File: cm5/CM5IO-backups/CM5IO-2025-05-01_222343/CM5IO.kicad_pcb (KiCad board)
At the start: 4 copper layers, 101.9 x 90.8 mm, 67 parts, among them J1 67910-5700, J14 JST_SHBM04B-SRSS-TB, J2 B2B-XH-A_LF__SN_, J4 0786463001, J5 USB3_A, J6 Conn_02x03_Counter_Clockwise, J7 Conn_01x04, U2 TLV320ADC6120IRTER, U5 74LVC1G07SE-7, U6 AP22653W6, U8 AP3441SHE-7B

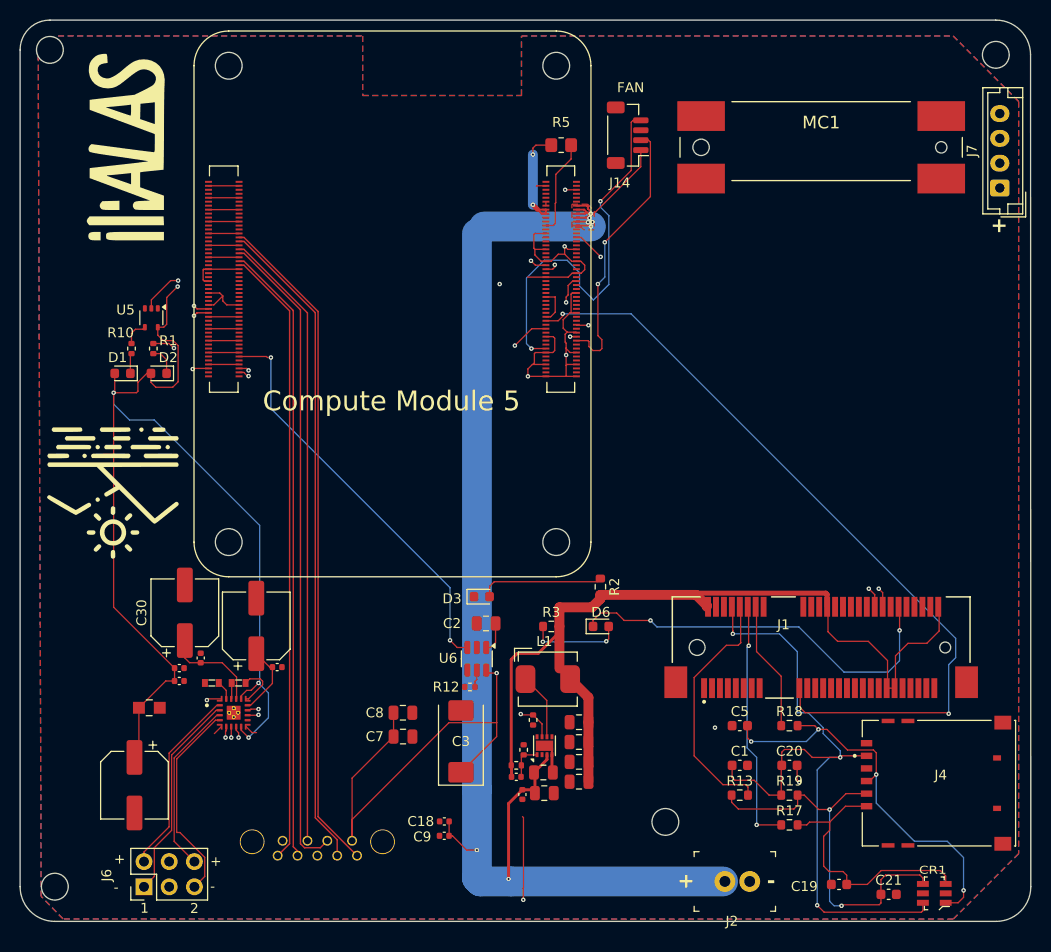
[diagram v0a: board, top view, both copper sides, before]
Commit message: Delete some unnecessary components and fix up some of the trace thicknesses
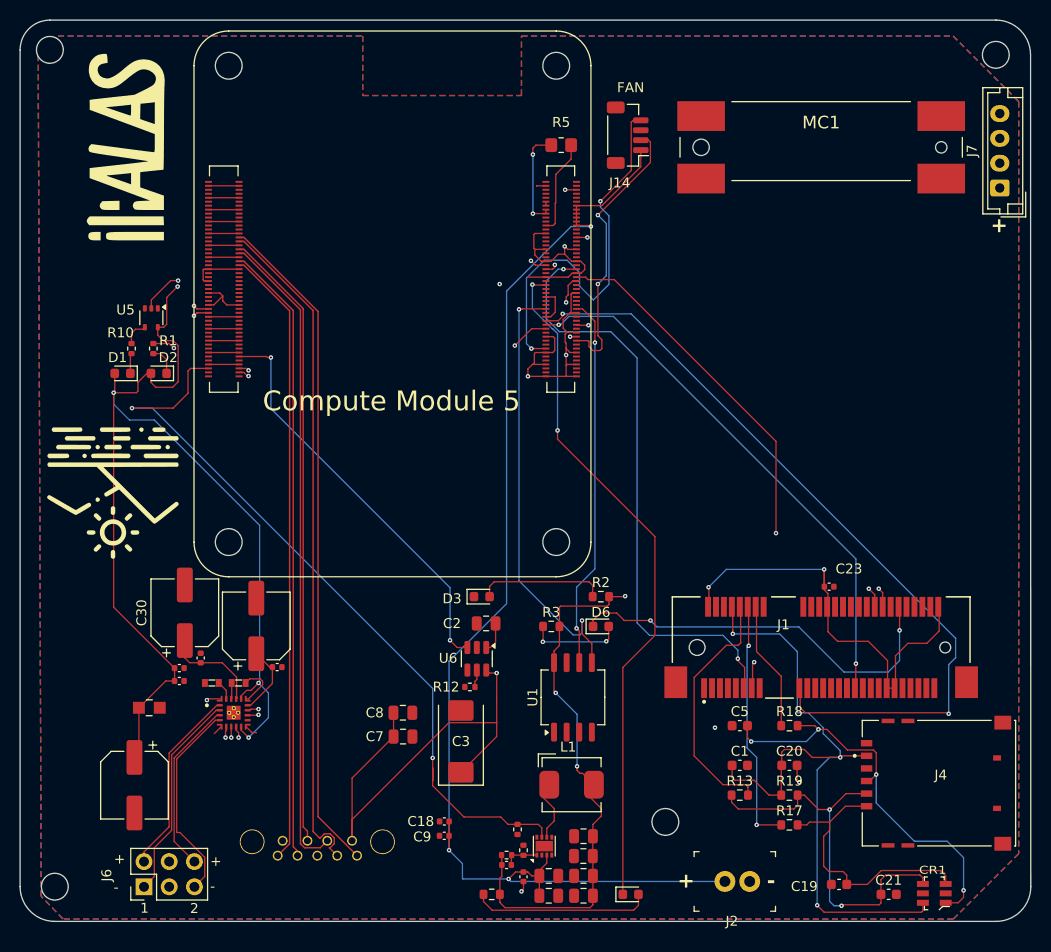
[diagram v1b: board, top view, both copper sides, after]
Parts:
- added C23: 100n, Capacitor_SMD:C_0402_1005Metric, F.Cu at (223.0, 126.0)
- added D4: LED Red, LED_SMD:LED_0603_1608Metric, F.Cu at (203.0, 157.0)
- added R11: 330, Resistor_SMD:R_0603_1608Metric, F.Cu at (189.0, 157.0)
- added U1: CAT24C128, Package_SO:SOIC-8_5.3x6.2mm_P1.27mm, F.Cu at (197.2, 137.2)
- moved C14 11.5 mm to (198.2, 151.1)
- moved C15 11.5 mm to (198.2, 157.1)
- moved C16 11.5 mm to (198.2, 155.1)
- moved C17 11.5 mm to (198.2, 153.1)
- moved R14 11.1 mm to (191.6, 150.5)
- moved L1 10.9 mm to (197.1, 145.9)
- moved C4 10.4 mm to (194.8, 155.1)
- moved C6 10.4 mm to (194.8, 157.1)
- moved R16 10.1 mm to (192.2, 152.6)
- moved U8 10.1 mm to (194.3, 152.1)
- moved R15 9.10 mm to (190.5, 153.0)
- moved C11 8.94 mm to (190.5, 154.0)
- moved C10 8.29 mm to (192.2, 155.2)
- moved R2 1.00 mm to (200.0, 127.0), turned to 0 degrees
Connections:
- J1 pad 11: unconnected-(J1-Pad11) -> /CM5_GPIO ( Ethernet, GPIO, SDCARD)/GPIO14
- J1 pad 13: unconnected-(J1-Pad13) -> /CM5_GPIO ( Ethernet, GPIO, SDCARD)/GPIO15
- J1 pad 31: /PCIe-M2/DTR -> /CM5_GPIO ( Ethernet, GPIO, SDCARD)/GPIO13
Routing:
- net /CM5_GPIO ( Ethernet, GPIO, SDCARD)/GPIO27: track 0.00 -> 69.3 mm, vias 0 -> 2
- net /CM5_GPIO ( Ethernet, GPIO, SDCARD)/GPIO14: track 0.00 -> 60.2 mm, vias 0 -> 2
- net /CM5_GPIO ( Ethernet, GPIO, SDCARD)/GPIO13: track 0.00 -> 54.8 mm, vias 0 -> 2
- net /CM5_GPIO ( Ethernet, GPIO, SDCARD)/GPIO15: track 0.00 -> 52.8 mm, vias 0 -> 2
- net /CM5_GPIO ( Ethernet, GPIO, SDCARD)/ID_SD: track 0.00 -> 44.7 mm, vias 0 -> 2
- net /CM5_GPIO ( Ethernet, GPIO, SDCARD)/ID_SC: track 0.00 -> 37.7 mm, vias 0 -> 2
- net /CM5_HighSpeed/PCIE_PWR_EN: track 54.0 -> 78.8 mm
- net Net-(D4-A): track 0.00 -> 18.0 mm
- net /+5v: track 140.8 -> 123.4 mm, vias 7 -> 3
- net GND: track 126.1 -> 113.2 mm
- net /PCIe-M2/M2_3v3: track 96.3 -> 108.1 mm, vias 0 -> 5
- net /CM5_GPIO ( Ethernet, GPIO, SDCARD)/DREG: track 7.25 -> 9.93 mm
- net Net-(U8-LX): track 6.71 -> 4.77 mm
- net /CM5_HighSpeed/USB3-1-TX_N: track 66.3 -> 68.0 mm
- net /+3.3v: track 161.7 -> 161.0 mm
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- removed copper zone on F.Cu, net /+5v
